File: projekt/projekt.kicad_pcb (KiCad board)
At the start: 2 copper layers, 100 x 40 mm, 53 parts, among them J1 Conn_01x05, J2 Conn_01x03, J4 87583-0010RHLF, J5 10118192-0001LF, U1 MAX17048G_T10, U2 TPS61022RWUT, U3 MCP73871-2CCI_ML

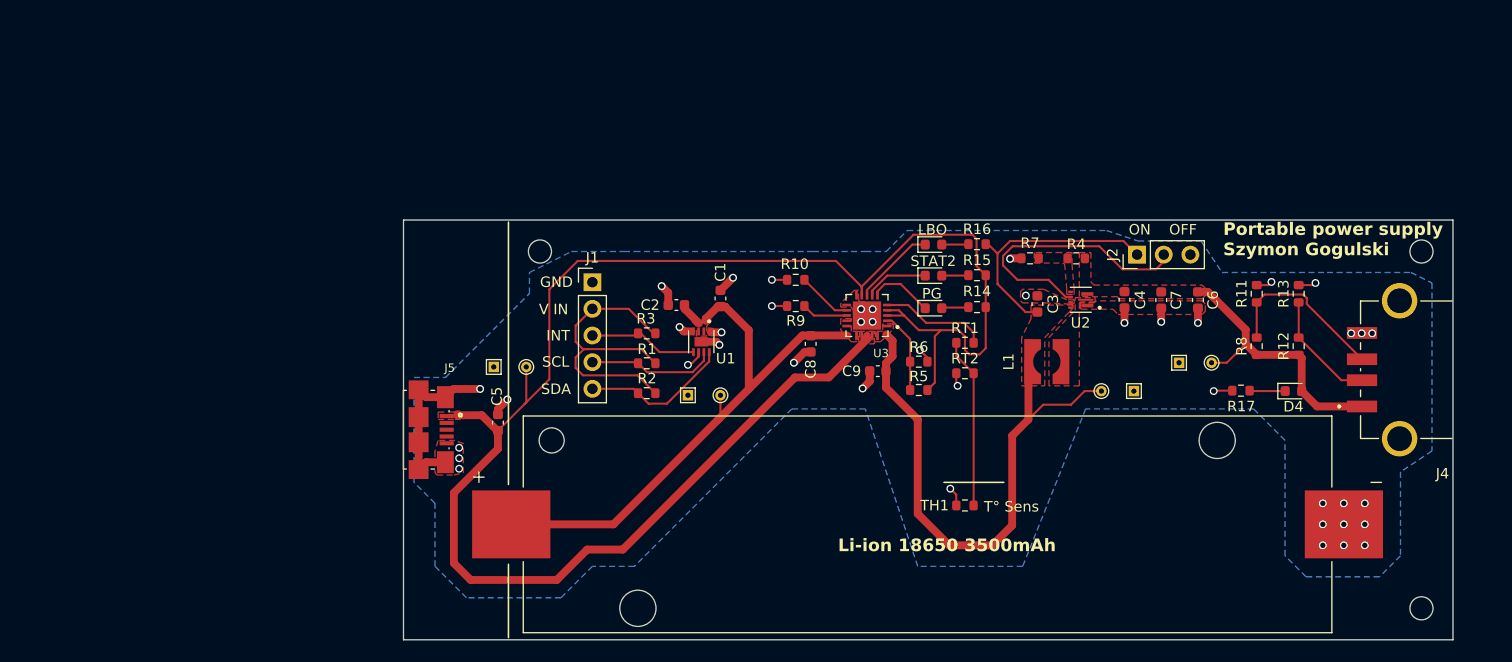
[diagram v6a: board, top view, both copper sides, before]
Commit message: MAIN: wersja 2: koniec, wysłane do produkcji.
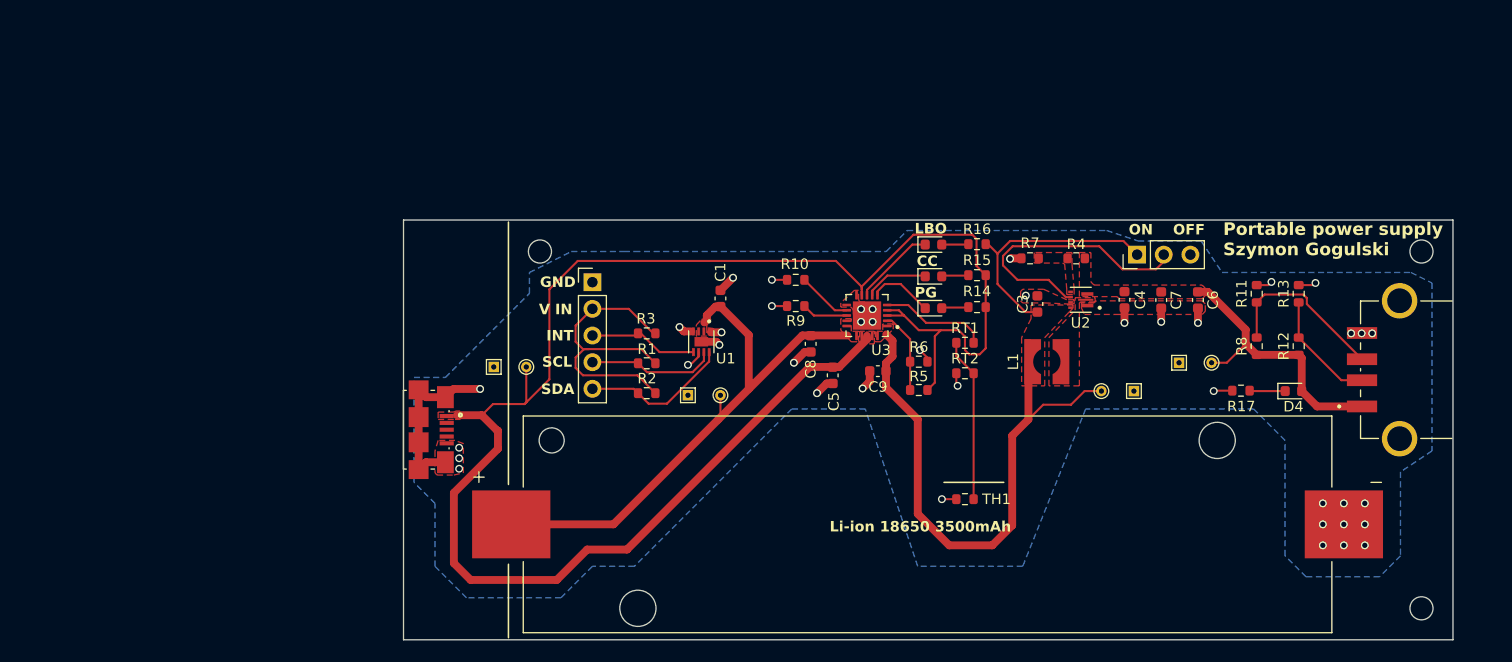
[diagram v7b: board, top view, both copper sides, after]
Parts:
- removed C2: 0.1u, Capacitor_SMD:C_0603_1608Metric
- moved C5 32.2 mm to (160.9, 74.8), turned to -90 degrees
- moved TH1 0.60 mm to (173.5, 86.6)
- moved D2 0.07 mm to (170.5, 65.4)
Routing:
- net GND: track 50.0 -> 47.6 mm, vias 42 -> 41
- net +BATT: track 55.5 -> 53.3 mm
- net +5V_CHARGE: track 164.7 -> 165.6 mm
- net Net-(RT1-Pad2): track 16.2 -> 15.6 mm
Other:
- board text added: "CC"
- board text added: "LBO - low battery output CC - charge complete PG - power good"
- board text added: "V IN - mcu logic voltage"
- board text removed: "STAT2"
- board text removed: "T° Sens"

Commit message: poprawki
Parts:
- D2: value LED Y -> LED G
- D3: value LED Y -> LED R
- R11, R13: value R -> 51k
- R12: value R -> 43k
- R8: value R -> 75k
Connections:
- net /STAT2 renamed /CC
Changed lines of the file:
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@@
   (net 8 "/INT")
   (net 9 "/PG")
-  (net 10 "/STAT2")
+  (net 10 "/CC")
   (net 11 "/D-")
   (net 12 "/D+")
@@
         (effects (font (size 1 1) (thickness 0.15)))
     )
-    (fp_text value "R" (at 0 1.43 90) (layer "F.Fab")
+    (fp_text value "51k" (at 0 1.43 90) (layer "F.Fab")
         (effects (font (size 1 1) (thickness 0.15)))
     )
@@
         (effects (font (size 1 1) (thickness 0.15)))
     )
-    (fp_text value "R" (at 0 1.43 90) (layer "F.Fab")
+    (fp_text value "43k" (at 0 1.43 90) (layer "F.Fab")
         (effects (font (size 1 1) (thickness 0.15)))
     )
@@
         (effects (font (size 1 1) (thickness 0.15)))
     )
-    (fp_text value "LED Y" (at 0 1.43) (layer "F.Fab")
+    (fp_text value "LED R" (at 0 1.43) (layer "F.Fab")
         (effects (font (size 1 1) (thickness 0.15)))
     )
@@
       (net 9 "/PG") (pinfunction "~{PG}") (pintype "output") (solder_mask_margin 0.102))
     (pad "7" smd roundrect (at -0.5 1.935 180) (size 0.26 0.84) (layers "F.Cu" "F.Paste" "F.Mask") (roundrect_rratio 0.25)
-      (net 10 "/STAT2") (pinfunction "STAT2") (pintype "output") (solder_mask_margin 0.102))
+      (net 10 "/CC") (pinfunction "STAT2") (pintype "output") (solder_mask_margin 0.102))
     (pad "8" smd roundrect (at 0 1.935 180) (size 0.26 0.84) (layers "F.Cu" "F.Paste" "F.Mask") (roundrect_rratio 0.25)
       (net 25 "/LBO") (pinfunction "STAT1/*LBO") (pintype "output") (solder_mask_margin 0.102))
@@
         (effects (font (size 1 1) (thickness 0.15)))
     )
-    (fp_text value "R" (at 0 1.43 90) (layer "F.Fab")
+    (fp_text value "75k" (at 0 1.43 90) (layer "F.Fab")
         (effects (font (size 1 1) (thickness 0.15)))
     )
@@
         (effects (font (size 1 1) (thickness 0.15)))
     )
-    (fp_text value "R" (at 0 1.43 90) (layer "F.Fab")
+    (fp_text value "51k" (at 0 1.43 90) (layer "F.Fab")
         (effects (font (size 1 1) (thickness 0.15)))
     )
@@
         (effects (font (size 1 1) (thickness 0.15)))
     )
-    (fp_text value "LED Y" (at 0 1.43) (layer "F.Fab")
+    (fp_text value "LED G" (at 0 1.43) (layer "F.Fab")
         (effects (font (size 1 1) (thickness 0.15)))
     )
@@
       (stroke (width 0.1) (type solid)) (layer "F.Fab"))
     (pad "1" smd roundrect (at -0.7875 0) (size 0.875 0.95) (layers "F.Cu" "F.Paste" "F.Mask") (roundrect_rratio 0.25)
-      (net 10 "/STAT2") (pinfunction "K") (pintype "passive"))
+      (net 10 "/CC") (pinfunction "K") (pintype "passive"))
     (pad "2" smd roundrect (at 0.7875 0) (size 0.875 0.95) (layers "F.Cu" "F.Paste" "F.Mask") (roundrect_rratio 0.25)
       (net 26 "Net-(D2-A)") (pinfunction "A") (pintype "passive"))
